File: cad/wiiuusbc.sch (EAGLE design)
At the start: 3 parts, among them J1 USB4105-GF-A

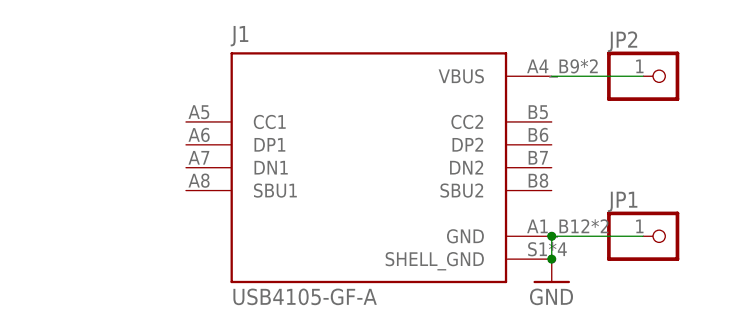
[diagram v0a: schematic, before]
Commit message: connect CC lines and update readme
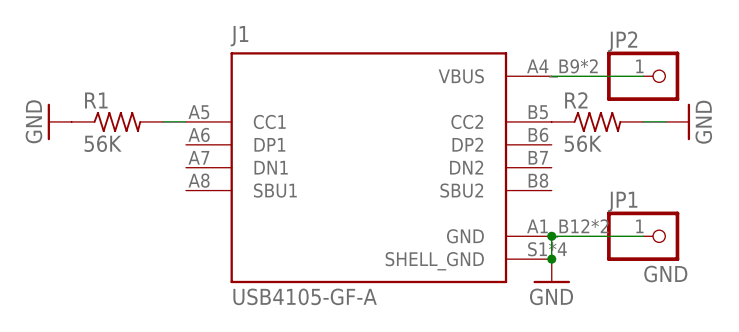
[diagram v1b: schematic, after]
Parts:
- added R1, R2: 56K, adafruit:R-US_R0402
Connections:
- new net CC1: J1.CC1, R1.2
- new net CC2: J1.CC2, R2.1
- net GND: now also R1.1, R2.2
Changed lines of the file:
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@@
 <part name="JP2" library="better14pin" deviceset="PINHD-1X1" device="" package3d_urn="urn:adsk.eagle:package:6240654/1"/>
 <part name="GND1" library="supply1" library_urn="urn:adsk.eagle:library:371" deviceset="GND" device=""/>
+<part name="R1" library="adafruit" deviceset="R-US_" device="R0402" value="56K"/>
+<part name="R2" library="adafruit" deviceset="R-US_" device="R0402" value="56K"/>
+<part name="GND2" library="supply1" library_urn="urn:adsk.eagle:library:371" deviceset="GND" device=""/>
+<part name="GND3" library="supply1" library_urn="urn:adsk.eagle:library:371" deviceset="GND" device=""/>
 </parts>
 <sheets>
@@
 <attribute name="VALUE" x="73.66" y="40.64" size="1.778" layer="96"/>
 </instance>
+<instance part="R1" gate="G$1" x="27.94" y="60.96" smashed="yes">
+<attribute name="NAME" x="24.13" y="62.4586" size="1.778" layer="95"/>
+<attribute name="VALUE" x="24.13" y="57.658" size="1.778" layer="96"/>
+</instance>
+<instance part="R2" gate="G$1" x="81.28" y="60.96" smashed="yes">
+<attribute name="NAME" x="77.47" y="62.4586" size="1.778" layer="95"/>
+<attribute name="VALUE" x="77.47" y="57.658" size="1.778" layer="96"/>
+</instance>
+<instance part="GND2" gate="1" x="20.32" y="60.96" smashed="yes" rot="R270">
+<attribute name="VALUE" x="17.78" y="63.5" size="1.778" layer="96" rot="R270"/>
+</instance>
+<instance part="GND3" gate="1" x="91.44" y="60.96" smashed="yes" rot="R90">
+<attribute name="VALUE" x="93.98" y="58.42" size="1.778" layer="96" rot="R90"/>
+</instance>
 </instances>
 <busses>
 </busses>
 <nets>
+<net name="CC1" class="0">
+<segment>
+<pinref part="J1" gate="G$1" pin="CC1"/>
+<pinref part="R1" gate="G$1" pin="2"/>
+<wire x1="33.02" y1="60.96" x2="35.56" y2="60.96" width="0.1524" layer="91"/>
+</segment>
+</net>
+<net name="CC2" class="0">
+<segment>
+<pinref part="J1" gate="G$1" pin="CC2"/>
+<pinref part="R2" gate="G$1" pin="1"/>
+</segment>
+</net>
 <net name="GND" class="0">
 <segment>
+<pinref part="R1" gate="G$1" pin="1"/>
+<pinref part="GND2" gate="1" pin="GND"/>
+</segment>
+<segment>
+<pinref part="J1" gate="G$1" pin="SHELL_GND"/>
+<pinref part="GND1" gate="1" pin="GND"/>
 <pinref part="J1" gate="G$1" pin="GND"/>
-<pinref part="J1" gate="G$1" pin="SHELL_GND"/>
-<wire x1="76.2" y1="48.26" x2="76.2" y2="45.72" width="0.1524" layer="91"/>
+<wire x1="76.2" y1="45.72" x2="76.2" y2="48.26" width="0.1524" layer="91"/>
+<junction x="76.2" y="45.72"/>
 <pinref part="JP1" gate="G$1" pin="1"/>
 <wire x1="76.2" y1="48.26" x2="86.36" y2="48.26" width="0.1524" layer="91"/>
 <junction x="76.2" y="48.26"/>
-<pinref part="GND1" gate="1" pin="GND"/>
-<junction x="76.2" y="45.72"/>
+<label x="86.36" y="43.18" size="1.778" layer="95"/>
+</segment>
+<segment>
+<pinref part="R2" gate="G$1" pin="2"/>
+<pinref part="GND3" gate="1" pin="GND"/>
+<wire x1="86.36" y1="60.96" x2="88.9" y2="60.96" width="0.1524" layer="91"/>
 </segment>
 </net>
